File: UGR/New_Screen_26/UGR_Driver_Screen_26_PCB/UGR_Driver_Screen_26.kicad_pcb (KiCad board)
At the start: 2 copper layers, 133.5 x 84 mm, 74 parts, among them J1 2171790001, J2 Conn_01x05, J3 Conn_02x20_Socket, J4 DF51-4DP-2DS_50_, J5 Conn_01x06, U1 TPS562200, U2 STM32F767VGTx, U3 LM358DT, U5 MCP2562-E-SN

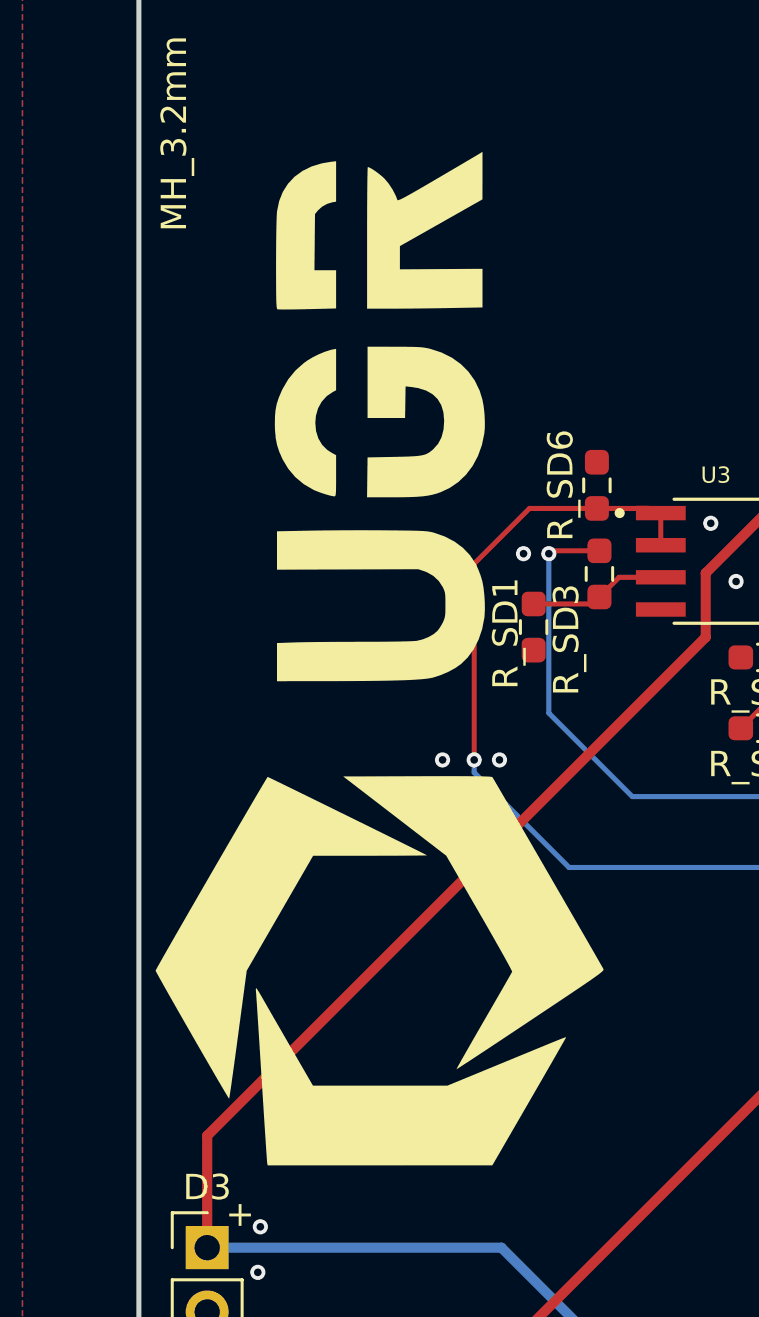
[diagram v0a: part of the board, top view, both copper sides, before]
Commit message: KiCad Library Overhaul
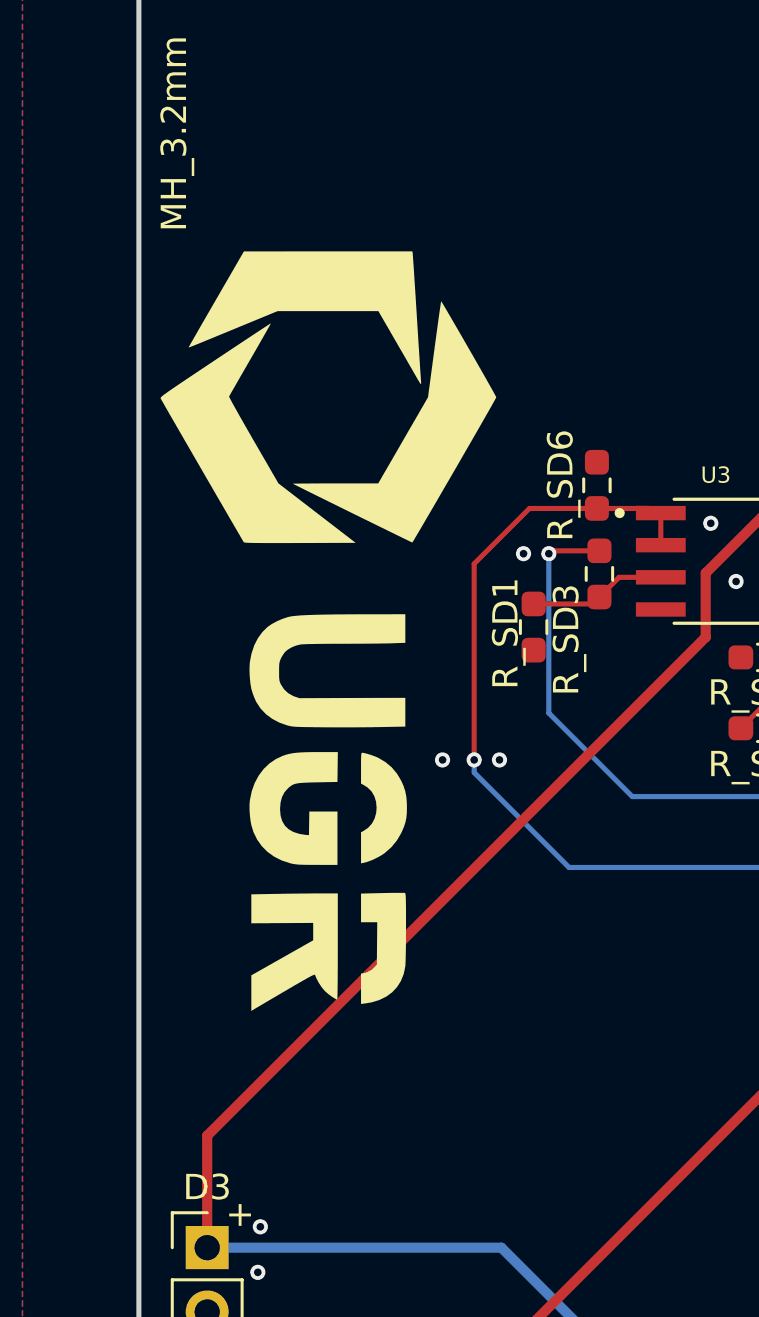
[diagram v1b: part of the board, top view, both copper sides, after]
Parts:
- removed the G*** at (89.5, 87.5)
- added G***: LOGO, UGR:UGR_ALL_SILK_30mm, F.Cu at (87.5, 86.4)
